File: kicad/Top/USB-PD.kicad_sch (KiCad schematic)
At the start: 0 parts

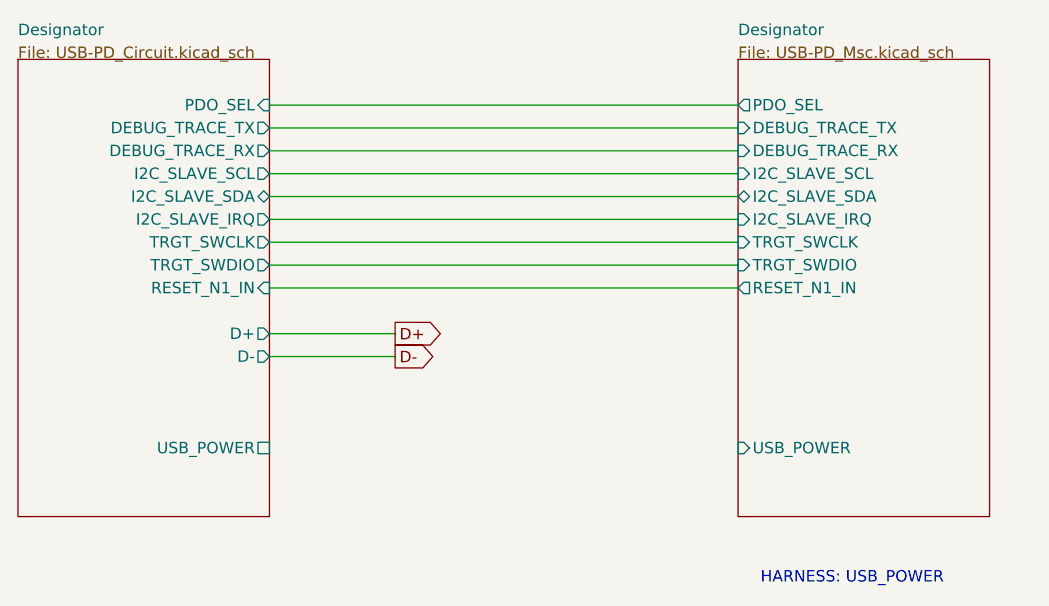
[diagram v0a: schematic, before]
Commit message: Renamed sheets
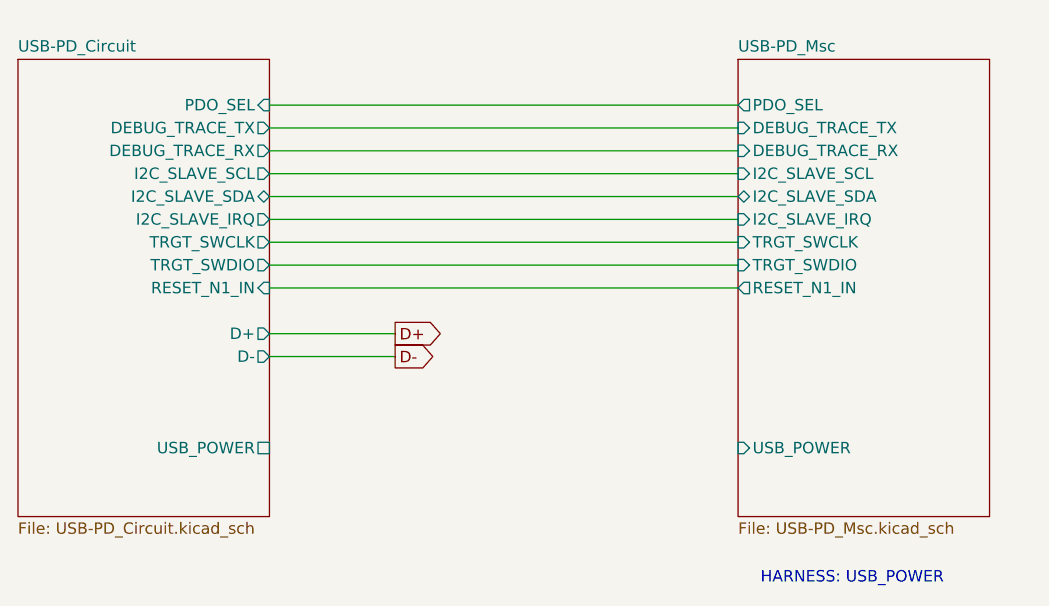
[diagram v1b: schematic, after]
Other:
- sheet Designator renamed USB-PD_Msc
- added sheet USB-PD_Circuit (USB-PD_Circuit.kicad_sch)
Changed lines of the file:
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@@
     (stroke (width 0) (type solid) (color 128 0 0 1))
     (fill (color 128 255 128 1.0000))
-    (property "Sheet name" "Designator" (id 0) (at 54.61 76.2 0)
+    (property "Sheet name" "USB-PD_Circuit" (id 0) (at 54.61 78.0284 0)
       (effects (font (size 1.27 1.27)) (justify left bottom))
     )
-    (property "Sheet file" "USB-PD_Circuit.kicad_sch" (id 1) (at 54.61 78.74 0)
-      (effects (font (size 1.27 1.27)) (justify left bottom))
+    (property "Sheet file" "USB-PD_Circuit.kicad_sch" (id 1) (at 54.61 130.1246 0)
+      (effects (font (size 1.27 1.27)) (justify left top))
     )
     (pin "TRGT_SWCLK" output (at 82.55 99.06 0)
@@
     (stroke (width 0) (type solid) (color 128 0 0 1))
     (fill (color 128 255 128 1.0000))
-    (property "Sheet name" "Designator" (id 0) (at 134.62 76.2 0)
+    (property "Sheet name" "USB-PD_Msc" (id 0) (at 134.62 78.0284 0)
       (effects (font (size 1.27 1.27)) (justify left bottom))
     )
-    (property "Sheet file" "USB-PD_Msc.kicad_sch" (id 1) (at 134.62 78.74 0)
-      (effects (font (size 1.27 1.27)) (justify left bottom))
+    (property "Sheet file" "USB-PD_Msc.kicad_sch" (id 1) (at 134.62 130.1246 0)
+      (effects (font (size 1.27 1.27)) (justify left top))
     )
     (pin "DEBUG_TRACE_RX" input (at 134.62 88.9 180)

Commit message: WIP, adding 3-pin pad symbol for smd R0 selection
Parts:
- added C? (x3): 1uF, symbol Device:C_Small
- added C?: 100nF, symbol Device:C_Small
- added C?: Capacitor NP, AltiumImports:_ALTIUM_WORK_00001_MCHP-CDB_Library_Database_MCHP-CDB.DbLib_Capacitor_CAP_C_0603, symbol Top-altium-import:1_Capacitor NP
- added C? (x2): Capacitor NP, AltiumImports:_ALTIUM_WORK_00001_MCHP-CDB_Library_Database_.._Footprints_CAP_C_0603.PcbLib_CAP_C_0603, symbol Top-altium-import:1_Capacitor NP
- added C? (x2): Capacitor NP, AltiumImports:_ALTIUM_WORK_00001_MCHP-CDB_Library_Database_MCHP-CDB.DbLib_Capacitor_CAP_C_0402, symbol Top-altium-import:1_Capacitor NP
- added D? (x2): ESDA25P35-1U1M, custom_modules:ESDA25P35-1U1M, symbol ESDA25P35-1U1M:ESDA25P35-1U1M
- added D?: LED_green, AltiumImports:_ALTIUM_WORK_00001_MCHP-CDB_Library_Database_.._Footprints_LED_0603_Green.PcbLib_LED_0603_GREEN, symbol Top-altium-import:3_LED_green
- added D?: ESDA25W, custom_modules:ESDA25W, symbol ESDA25W:ESDA25W
- added J?: USBC_Receptacle_SMD_RA, AltiumImports:CON_USB3.1-C_RCPT_SMD_RA_ACP_12401610E4#2A, symbol Top-altium-import:0_mirrored_USBC_Receptacle_SMD_RA
- added J?: M20-9990246, AltiumImports:FP-M20-9990246-MFG, symbol Top-altium-import:3_mirrored_3bc925449376181038e59eaffc5286c
- added JP? (x2): 3-pad-selection, symbol custom_connectors:3-pad-selection
- added Q?: SI4477DY-T1-GE3, AltiumImports:_ALTIUM_WORK_00001_MCHP-CDB_Library_Database_.._Footprints_SOIC-8.PcbLib_SOIC-8, symbol Top-altium-import:1_SI4477DY-T1-GE3
- added Q?: SI4477DY-T1-GE3, AltiumImports:_ALTIUM_WORK_00001_MCHP-CDB_Library_Database_.._Footprints_SOIC-8.PcbLib_SOIC-8, symbol Top-altium-import:1_mirrored_SI4477DY-T1-GE3
- added R?: 1k, symbol Device:R_Small_US
- added R?: 100, symbol Device:R_Small_US
- added R?: CRGP0402F10K, AltiumImports:FP-CRGP0402-IPC_A, symbol Top-altium-import:2_CMP-03211-008310-1
- added R? (x2): 0, symbol Device:R_Small_US
- added R?: Resistor, AltiumImports:_ALTIUM_WORK_00001_MCHP-CDB_Library_Database_MCHP-CDB.DbLib_Resistor_RES_C_0402, symbol Top-altium-import:2_Resistor
- added R? (x2): 100k, symbol Device:R_Small_US
- added R?: Resistor, AltiumImports:_ALTIUM_WORK_00001_MCHP-CDB_Library_Database_.._Footprints_RES_C_0402.PcbLib_RES_C_0402, symbol Top-altium-import:1_Resistor
- added R?: 10K, symbol Device:R_Small_US
- added R?: 22k, symbol Device:R_Small_US
- added R?: Resistor, AltiumImports:_ALTIUM_WORK_00001_MCHP-CDB_Library_Database_.._Footprints_RES_C_0402.PcbLib_RES_C_0402, symbol Top-altium-import:0_Resistor
- added TP? (x2): Test Point No BOM, AltiumImports:_ALTIUM_WORK_00001_MCHP-CDB_Library_Database_.._Footprints_TP_1mm_SMD.PcbLib_TP_1mm_SMD, symbol Top-altium-import:0_Test Point No BOM
- added TP?: Test Point No BOM, AltiumImports:_ALTIUM_WORK_00001_MCHP-CDB_Library_Database_.._Footprints_TP_1mm_SMD.PcbLib_TP_1mm_SMD, symbol Top-altium-import:1_Test Point No BOM
- added TP?: Test Point No BOM, AltiumImports:_ALTIUM_WORK_00001_MCHP-CDB_Library_Database_.._Footprints_TP_1mm_SMD.PcbLib_TP_1mm_SMD, symbol Top-altium-import:3_Test Point No BOM
- added U3: MCP1804 SOT-23-5, AltiumImports:_ALTIUM_WORK_00001_MCHP-CDB_Library_Database_MCHP-CDB.DbLib_MCHP-Analog_SOT-23-5, symbol Top-altium-import:0_MCP1804 SOT-23-5
- added U?: STUSB4500BJR, custom_modules:STUSB4500BJR, symbol STUSB4500BJR:STUSB4500BJR
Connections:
- net D+: now also J?.A6 (D+), J?.B6 (D+), TP?.1
- net D-: now also J?.A7 (D-), J?.B7 (D-), TP?.1
- new net: C?.2, D?.1, J?.A4 (VBUS), J?.A9 (VBUS), J?.B4 (VBUS), J?.B9 (VBUS), Q?.5 (D), Q?.6 (D), Q?.7 (D), Q?.8 (D), R?.1
- new net: R?.2, U?.A1 (VBUS_VS__DISCH)
- new net: Q?.4 (G), Q?.4 (G), R?.1, R?.1, R?.2
- new net: C?.2, R?.2
- new net: R?.1, U3.4 (~{SHDN)
- new net: C?.2, R?.2, U3.1 (VIN)
- new net: JP?.2, R?.1, R?.1, U?.D3 (ADDR0)
- new net: D?.1 (A), R?.1
- new net: C?.2, U?.A3 (VREG__1V2)
- new net: R?.1, U?.C1 (VBUS__EN_SNK)
- new net: JP?.2, R?.1, R?.1, U?.D2 (ADDR1)
- new net: R?.1, U?.E4 (DISCH)
- new net 2V7: C?.2, U?.A4 (VREG__2V7)
- new net 3V3U3: C?.2, R?.2, U3.5 (VOUT)
- new net AGND: C?.1, C?.1, C?.1, C?.1, C?.1, D?.3, JP?.1, JP?.1, R?.1, R?.2, R?.2, R?.2, R?.2, U?.B3 (NC), U?.C3 (NC), U?.E3 (GND)
- new net CC1: C?.2, D?.2, J?.A5 (CC1), TP?.1, U?.B4 (CC1DB), U?.B5 (CC1)
- new net CC2: C?.2, D?.1, J?.B5 (CC2), TP?.1, U?.C4 (CC2DB), U?.C5 (CC2)
- new net PGND: C?.1, C?.1, C?.1, D?.2, D?.2, D?.2 (K), J?.25 (SHLD), J?.A1 (GND), J?.A12 (GND), J?.B1 (GND), J?.B12 (GND), U3.2 (GND)
- new net STUSB_ALERT: U?.B2 (ALERT)
- new net STUSB_RESET: R?.2, U?.D4 (RESET)
- new net STUSB_SCL: U?.D5 (SCL)
- new net STUSB_SDA: U?.E5 (SDA)
- new net VBUS_F: C?.2, Q?.1 (S), Q?.1 (S), Q?.2 (S), Q?.2 (S), Q?.3 (S), Q?.3 (S), R?.2, U?.A5 (VDD)
- new net VBUS_USB: J?.1
- new net VBUS_USB_OUT: J?.2
- new net VCC: JP?.3, JP?.3, U?.B1 (VSYS)
- new net VSNK: C?.1, D?.1, Q?.5 (D), Q?.6 (D), Q?.7 (D), Q?.8 (D), R?.2
- no-connect marks 0 -> 12
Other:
- removed sheet USB-PD_Circuit
- removed sheet USB-PD_Msc
- note added: ""PWR_IN""
- note added: ""PWR_OUT""
- note added: "+"
- note added: "3V3 @ 150mA"
- note added: "PWR"
- note added: "Power Output"
- note added: "Upstream Facing Port (UFP)"
- note added: "VBUS (5-20VDC) to 3.3VDC"
- note removed: "HARNESS: USB_POWER"
